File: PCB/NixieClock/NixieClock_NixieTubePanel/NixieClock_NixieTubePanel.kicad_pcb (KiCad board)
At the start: 2 copper layers, 112 x 112 mm, 31 parts, among them J3 Conn_01x04_Pin, J4 Conn_01x04_Pin, U1 K155ID1, U2 K155ID1, U3 K155ID1, U4 K155ID1, U5 PCF8574, U6 PCF8574, X1 5230, X2 5230, X3 5230, X4 5230, X5 5230, X6 5230

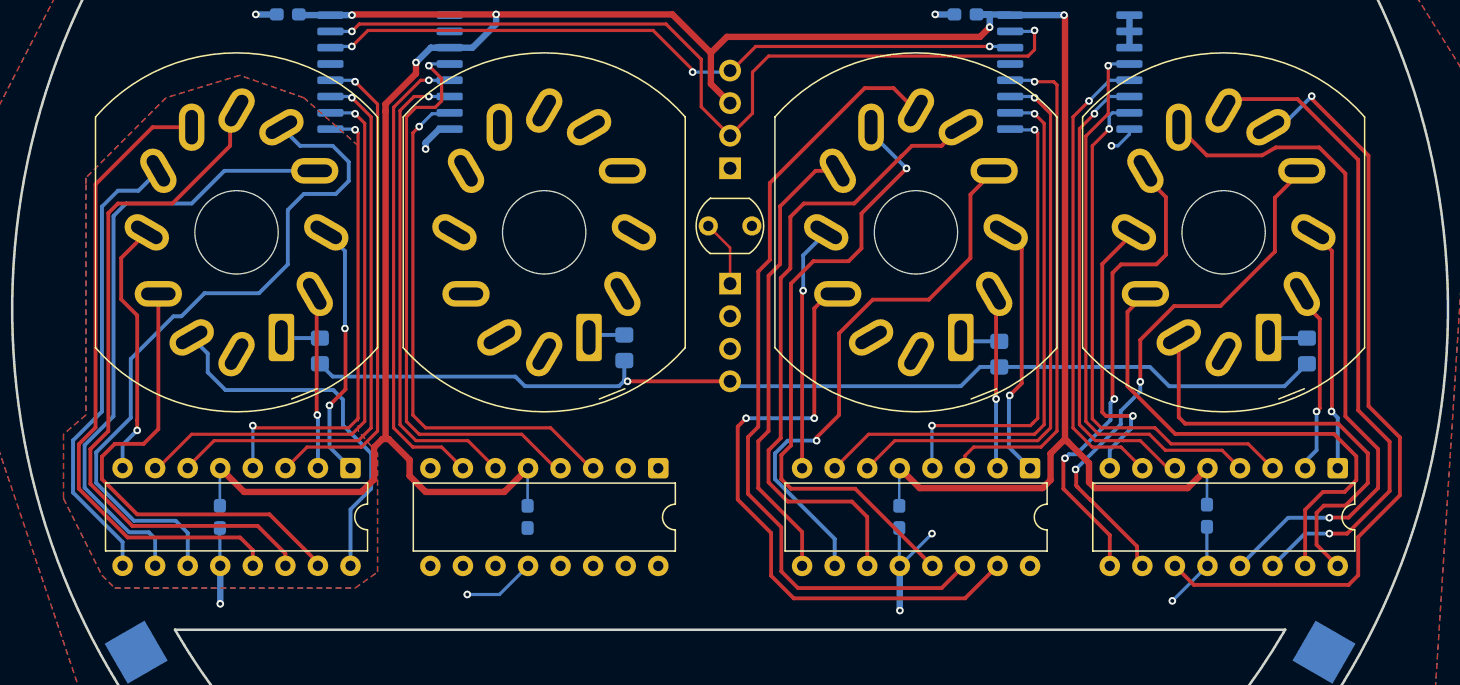
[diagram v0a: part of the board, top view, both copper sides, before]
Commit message: complete tube 2 wiring
complete trace layout for tube 2 on top and bot side
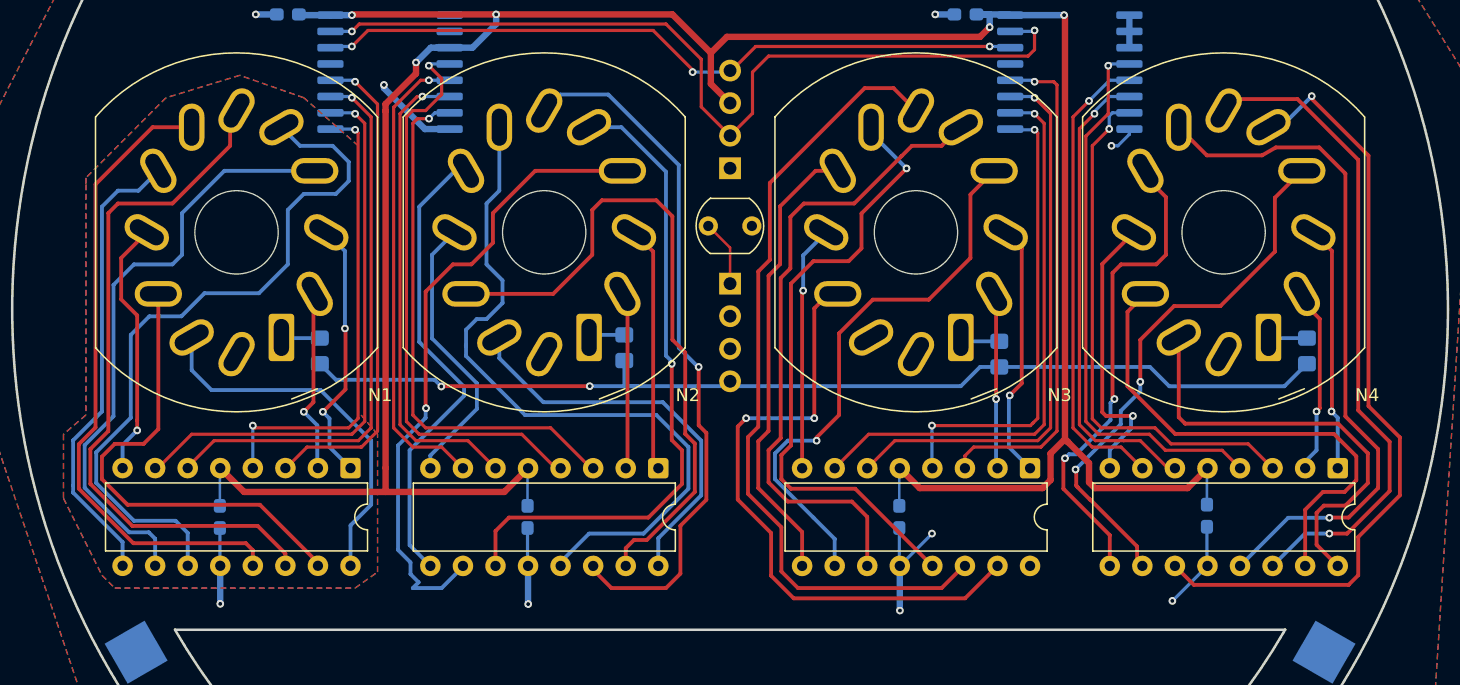
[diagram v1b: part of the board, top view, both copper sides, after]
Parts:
- N1, N2, N3, N4: footprint TerminalCuriosityFootprints:in-12_nixie-tube -> TerminalCuriosityFootprints:in-12_nixie-tube-socket
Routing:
- net Net-(N2-'5'): track 0.00 -> 56.6 mm
- net Net-(N2-'6'): track 1.17 -> 56.3 mm, vias 0 -> 1
- net Net-(N2-'2'): track 0.00 -> 52.5 mm
- net Net-(N2-'7'): track 0.00 -> 51.1 mm, vias 0 -> 1
- net Net-(N2-'8'): track 0.13 -> 50.3 mm, vias 0 -> 1
- net Net-(N2-'4'): track 0.00 -> 36.9 mm
- net Net-(N2-'1'): track 0.00 -> 31.2 mm
- net Net-(N2-'3'): track 0.17 -> 22.2 mm
- net Net-(N2-'9'): track 0.46 -> 19.6 mm
- net Net-(N2-'0'): track 0.71 -> 14.5 mm
- net GND: track 39.6 -> 43.8 mm
- net Net-(N1-'8'): track 48.7 -> 47.4 mm
- net +5V: track 215.5 -> 214.3 mm
- net Net-(N1-'7'): track 55.7 -> 56.8 mm
- net Net-(N1-'0'): track 13.5 -> 14.4 mm
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
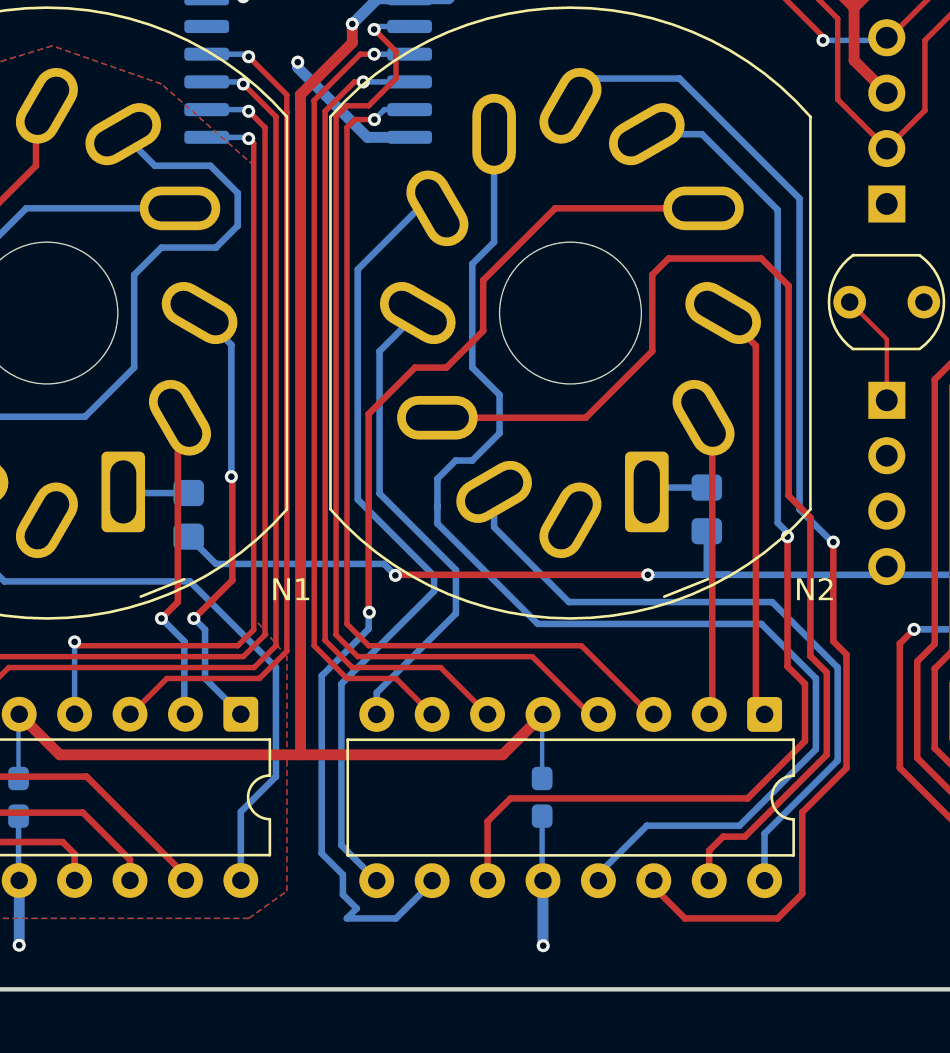
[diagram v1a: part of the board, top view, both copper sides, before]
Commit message: tube 2 checkpoint
tubes 1 and 2 have been routed using top/bot traces. saving checkpoint before rerouting tube 3 the same
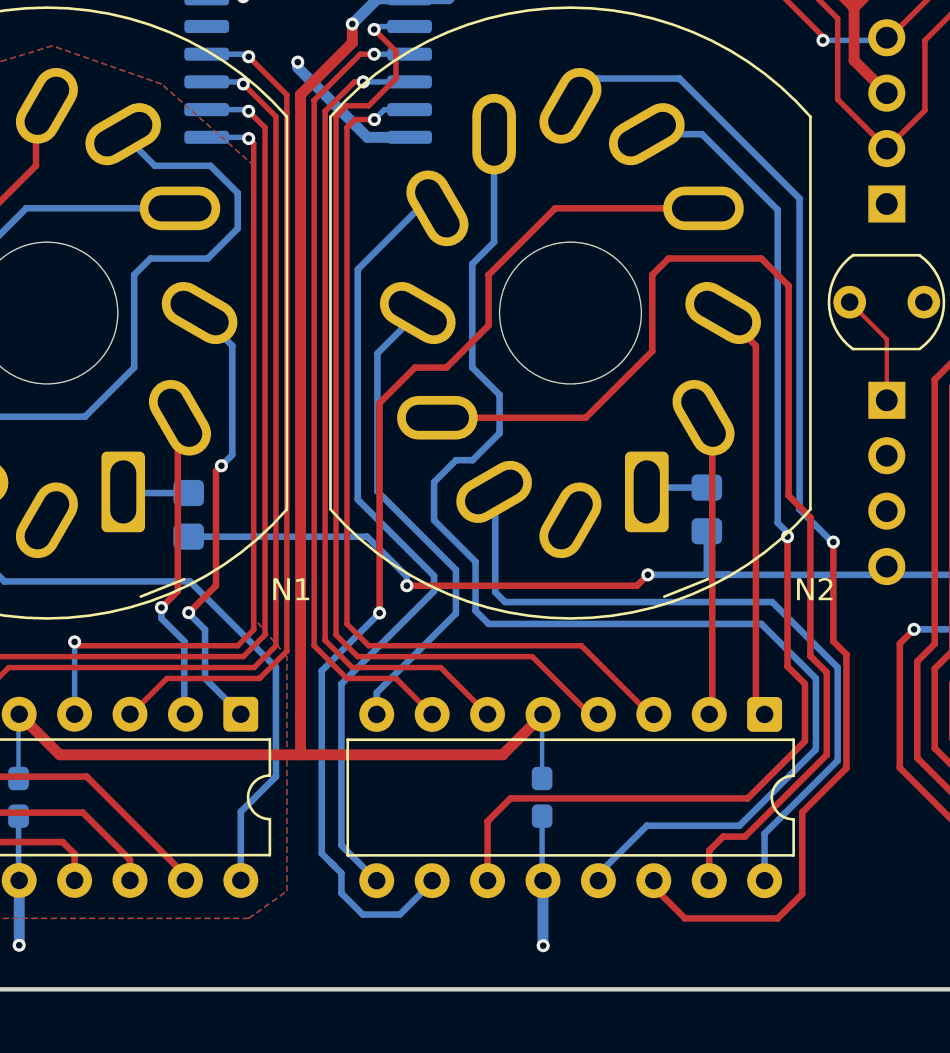
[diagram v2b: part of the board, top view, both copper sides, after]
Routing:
- net Net-(N2-'1'): track 31.2 -> 32.9 mm
- net Net-(N2-'5'): track 56.6 -> 58.0 mm
- net Net-(N2-'8'): track 50.3 -> 49.5 mm
- net /+170V: track 83.9 -> 84.5 mm

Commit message: Tube 3 wiring complete
Tube 3 wiring top/bot complete. tube 4 started
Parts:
- moved R11 10.9 mm to (140.2, 105.5), turned to 180 degrees
- moved R16 10.6 mm to (164.8, 106.0), turned to 180 degrees
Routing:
- net Net-(N4-'7'): track 61.2 -> 0.95 mm, vias 1 -> 0
- net Net-(N4-'6'): track 51.5 -> 0.26 mm, vias 1 -> 0
- net Net-(N4-'5'): track 53.8 -> 3.80 mm, vias 1 -> 0
- net Net-(N4-'8'): track 42.5 -> 0.00 mm, vias 2 -> 0
- net Net-(N4-'2'): track 39.1 -> 0.00 mm
- net Net-(N4-'4'): track 38.4 -> 2.65 mm, vias 2 -> 0
- net Net-(N4-'1'): track 34.2 -> 0.00 mm
- net Net-(N3-'1'): track 0.00 -> 29.0 mm, vias 0 -> 1
- net Net-(N4-'3'): track 22.5 -> 2.27 mm, vias 1 -> 0
- net Net-(N4-'9'): track 19.2 -> 0.00 mm, vias 1 -> 0
- net Net-(N1-'9'): track 20.8 -> 37.7 mm, vias 2 -> 1
- net Net-(N4-'0'): track 14.7 -> 0.00 mm, vias 1 -> 0
- net /+170V: track 84.5 -> 75.0 mm, vias 2 -> 5
- net Net-(N3-'2'): track 49.3 -> 40.0 mm, vias 2 -> 0
- net Net-(N1-'7'): track 56.8 -> 50.1 mm, vias 0 -> 1
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
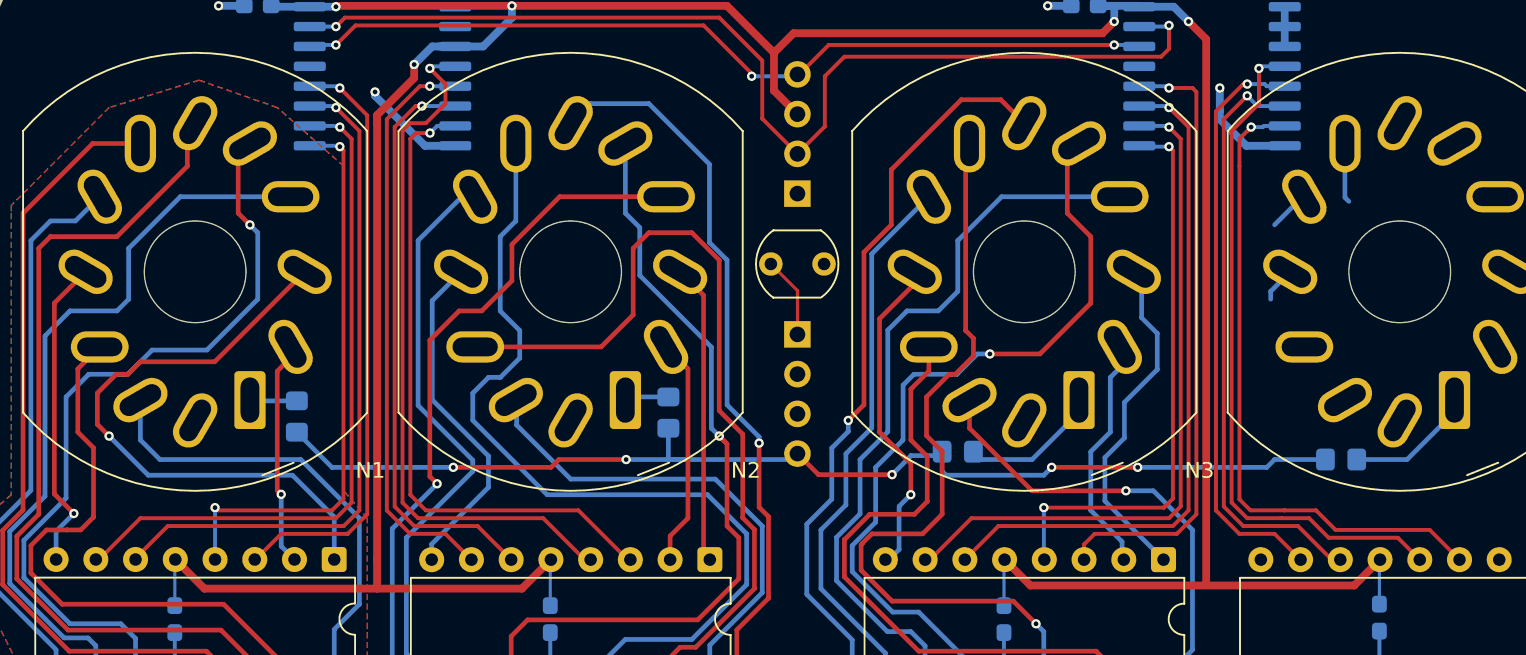
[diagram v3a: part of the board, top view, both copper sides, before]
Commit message: Tidied U1 and U3 connections
adjust pin ordering on U1 and U3 in schematic so they would connect to the PCF chips neater on the PCB without needing vias
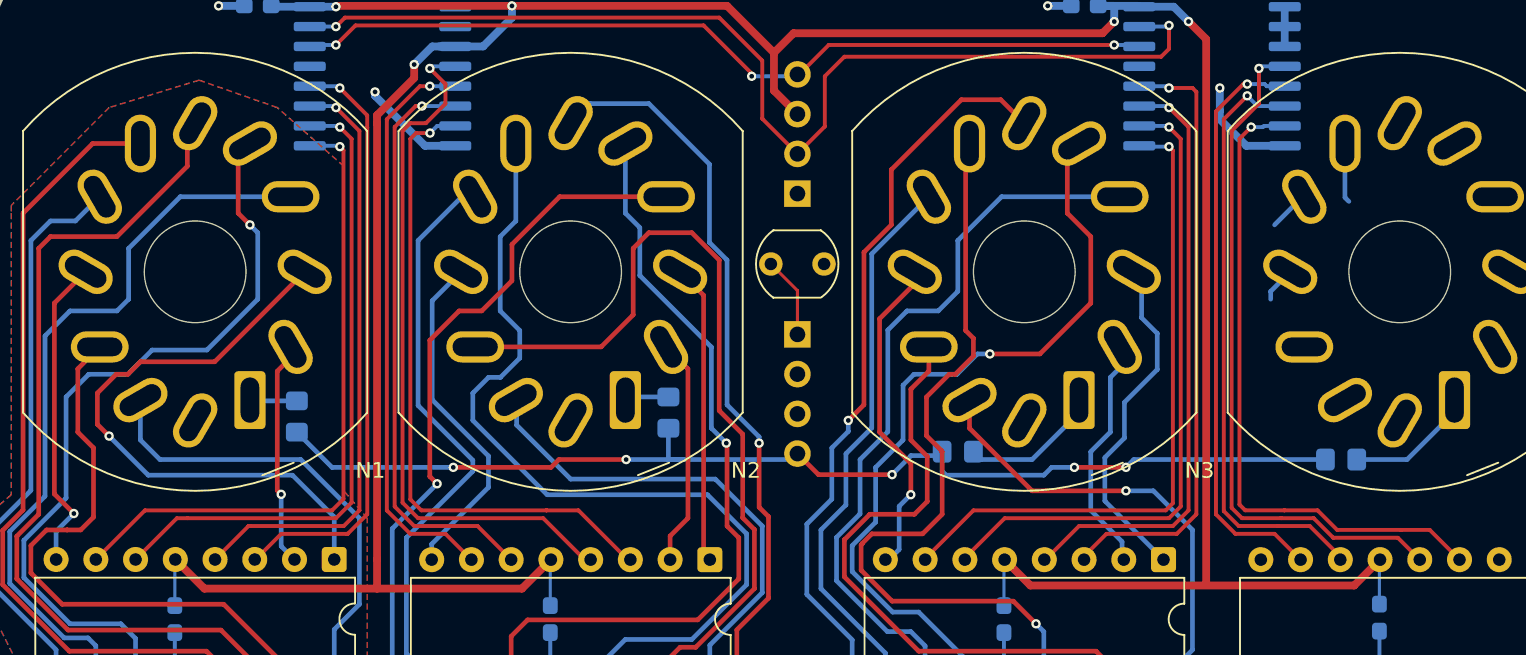
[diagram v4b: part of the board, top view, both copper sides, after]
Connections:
- U5 pad 10: Net-(U1-C) -> Net-(U1-B)
- U5 pad 11: Net-(U1-B) -> Net-(U1-D)
- U5 pad 9: Net-(U1-D) -> Net-(U1-C)
- U6 pad 10: Net-(U3-C) -> Net-(U3-B)
- U6 pad 11: Net-(U3-B) -> Net-(U3-D)
- U6 pad 9: Net-(U3-D) -> Net-(U3-C)
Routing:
- net Net-(U3-D): track 36.6 -> 38.8 mm, vias 2 -> 1
- net Net-(U1-D): track 36.5 -> 38.6 mm, vias 2 -> 1
- net Net-(U1-B): track 43.7 -> 41.7 mm
- net Net-(U3-B): track 43.8 -> 41.8 mm
- net Net-(U1-C): track 44.1 -> 42.2 mm
- net Net-(U3-C): track 44.2 -> 42.7 mm
- net Net-(N2-'7'): track 50.3 -> 49.6 mm

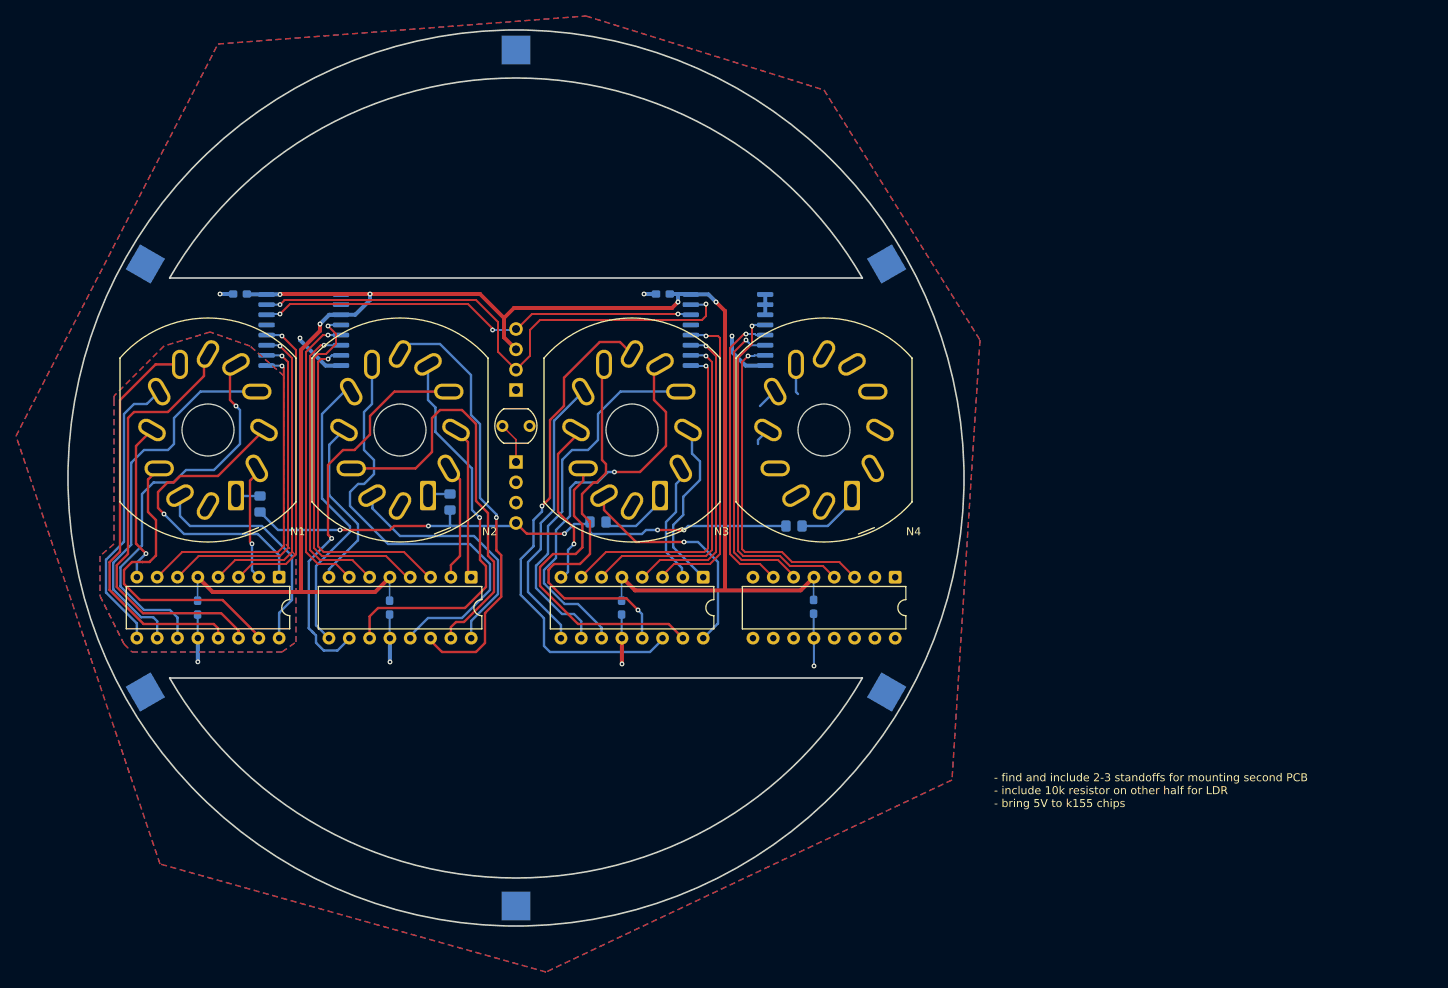
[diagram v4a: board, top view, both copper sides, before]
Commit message: change driver 3 ground trace to back side
rerouted some traces so that driver chip 3 ground trace can run on the back instead of the front, which looks neater and matches the other 3 chips
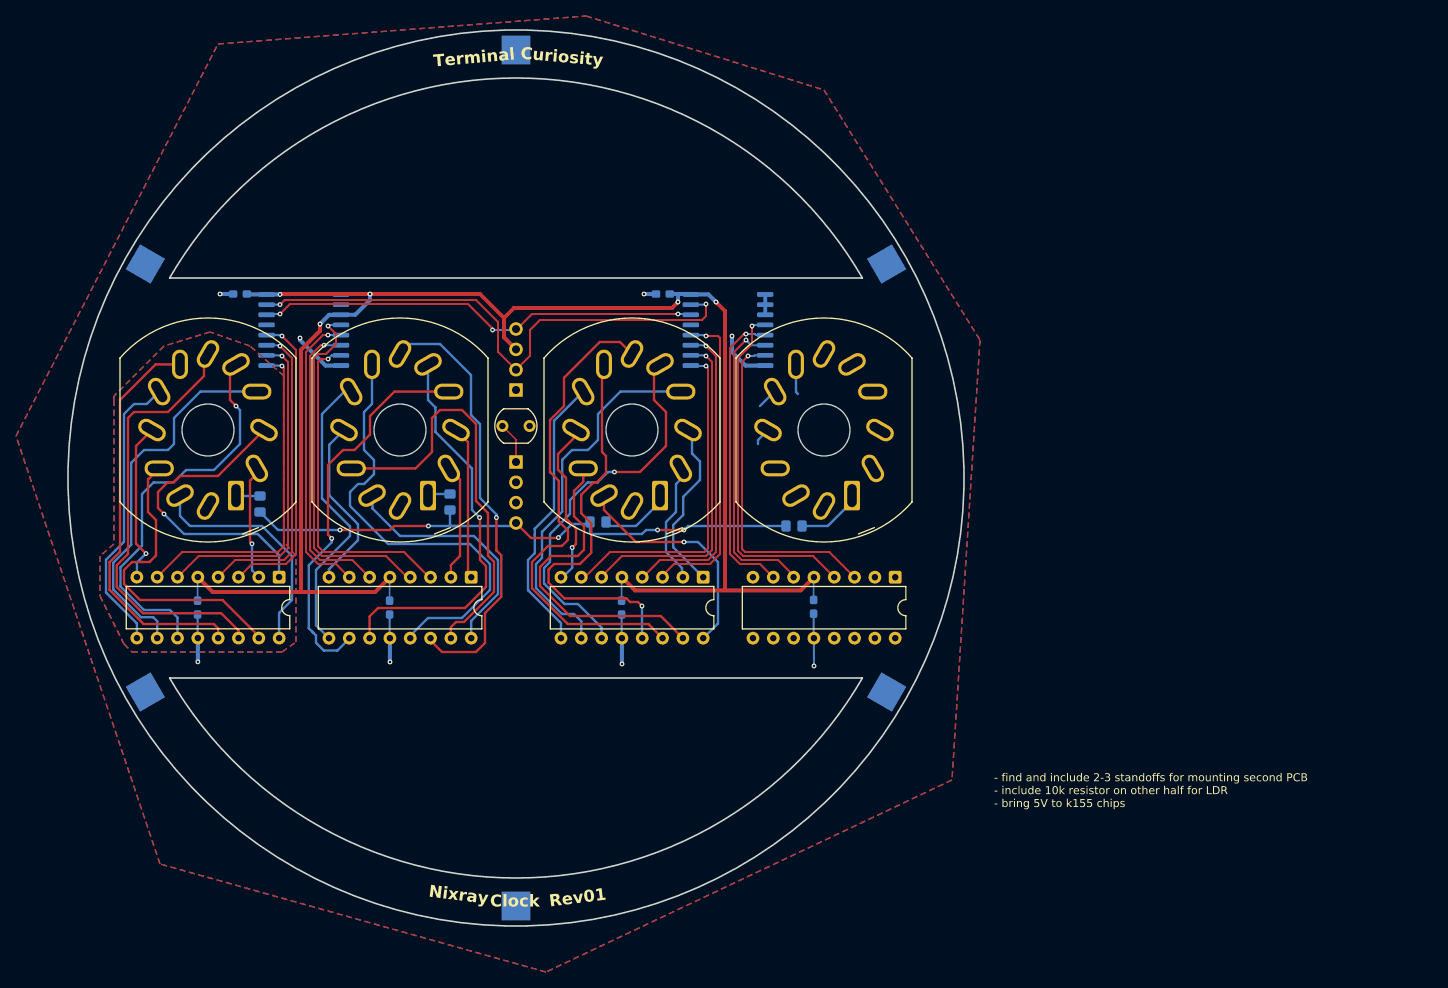
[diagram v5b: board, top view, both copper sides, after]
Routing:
- net Net-(N3-'6'): track 63.9 -> 60.7 mm, vias 1 -> 0
- net Net-(N3-'7'): track 49.4 -> 48.5 mm
- net Net-(N3-'5'): track 50.3 -> 51.1 mm
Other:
- board text added: "Clock"
- board text added: "Nixray"
- board text removed: "DDMMMYYYY"
- board text removed: "Display"
- board text removed: "Nixie"
- board text removed: "PCBA"
- board text removed: "Tube"
